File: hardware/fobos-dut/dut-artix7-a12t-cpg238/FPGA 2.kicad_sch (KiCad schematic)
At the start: 7 parts

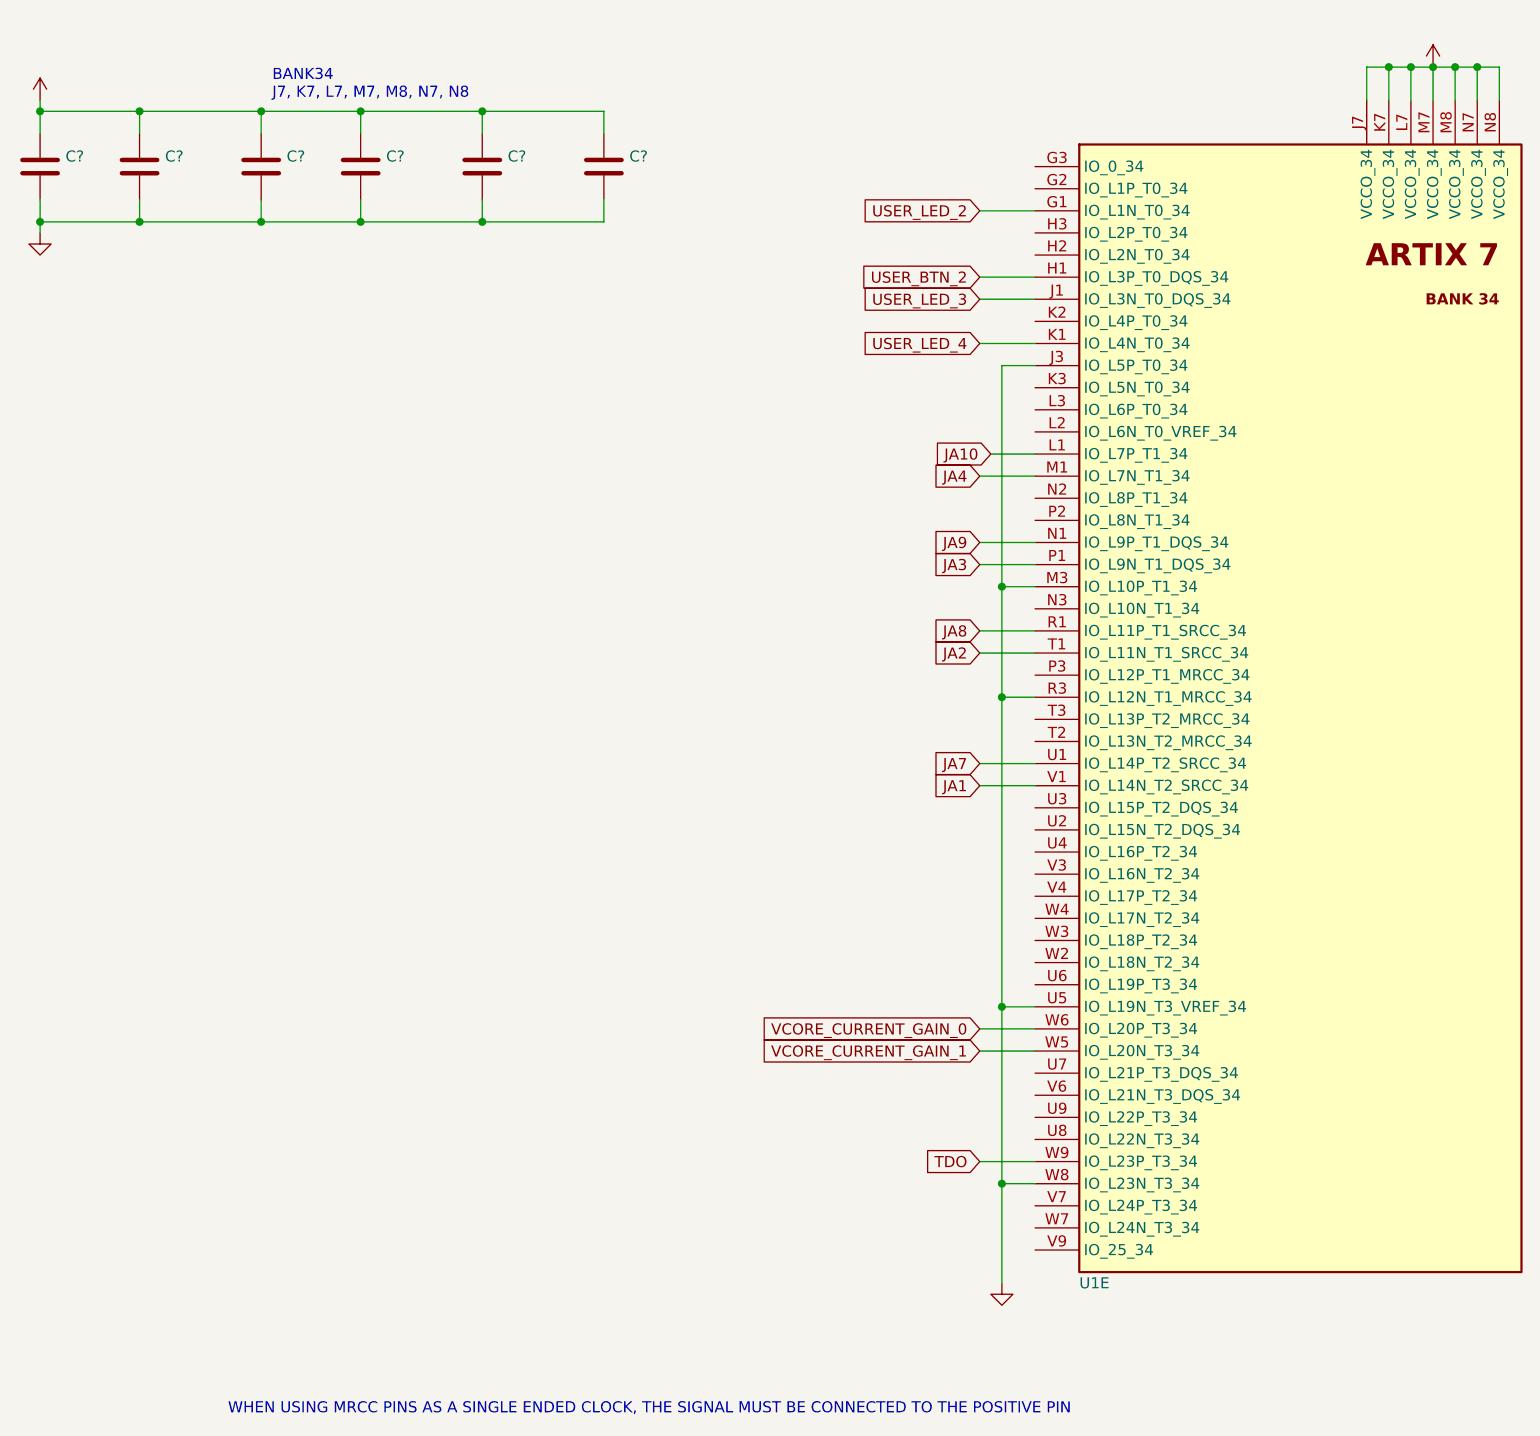
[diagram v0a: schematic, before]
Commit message: transitioned artix-7 dut to Kikad 6
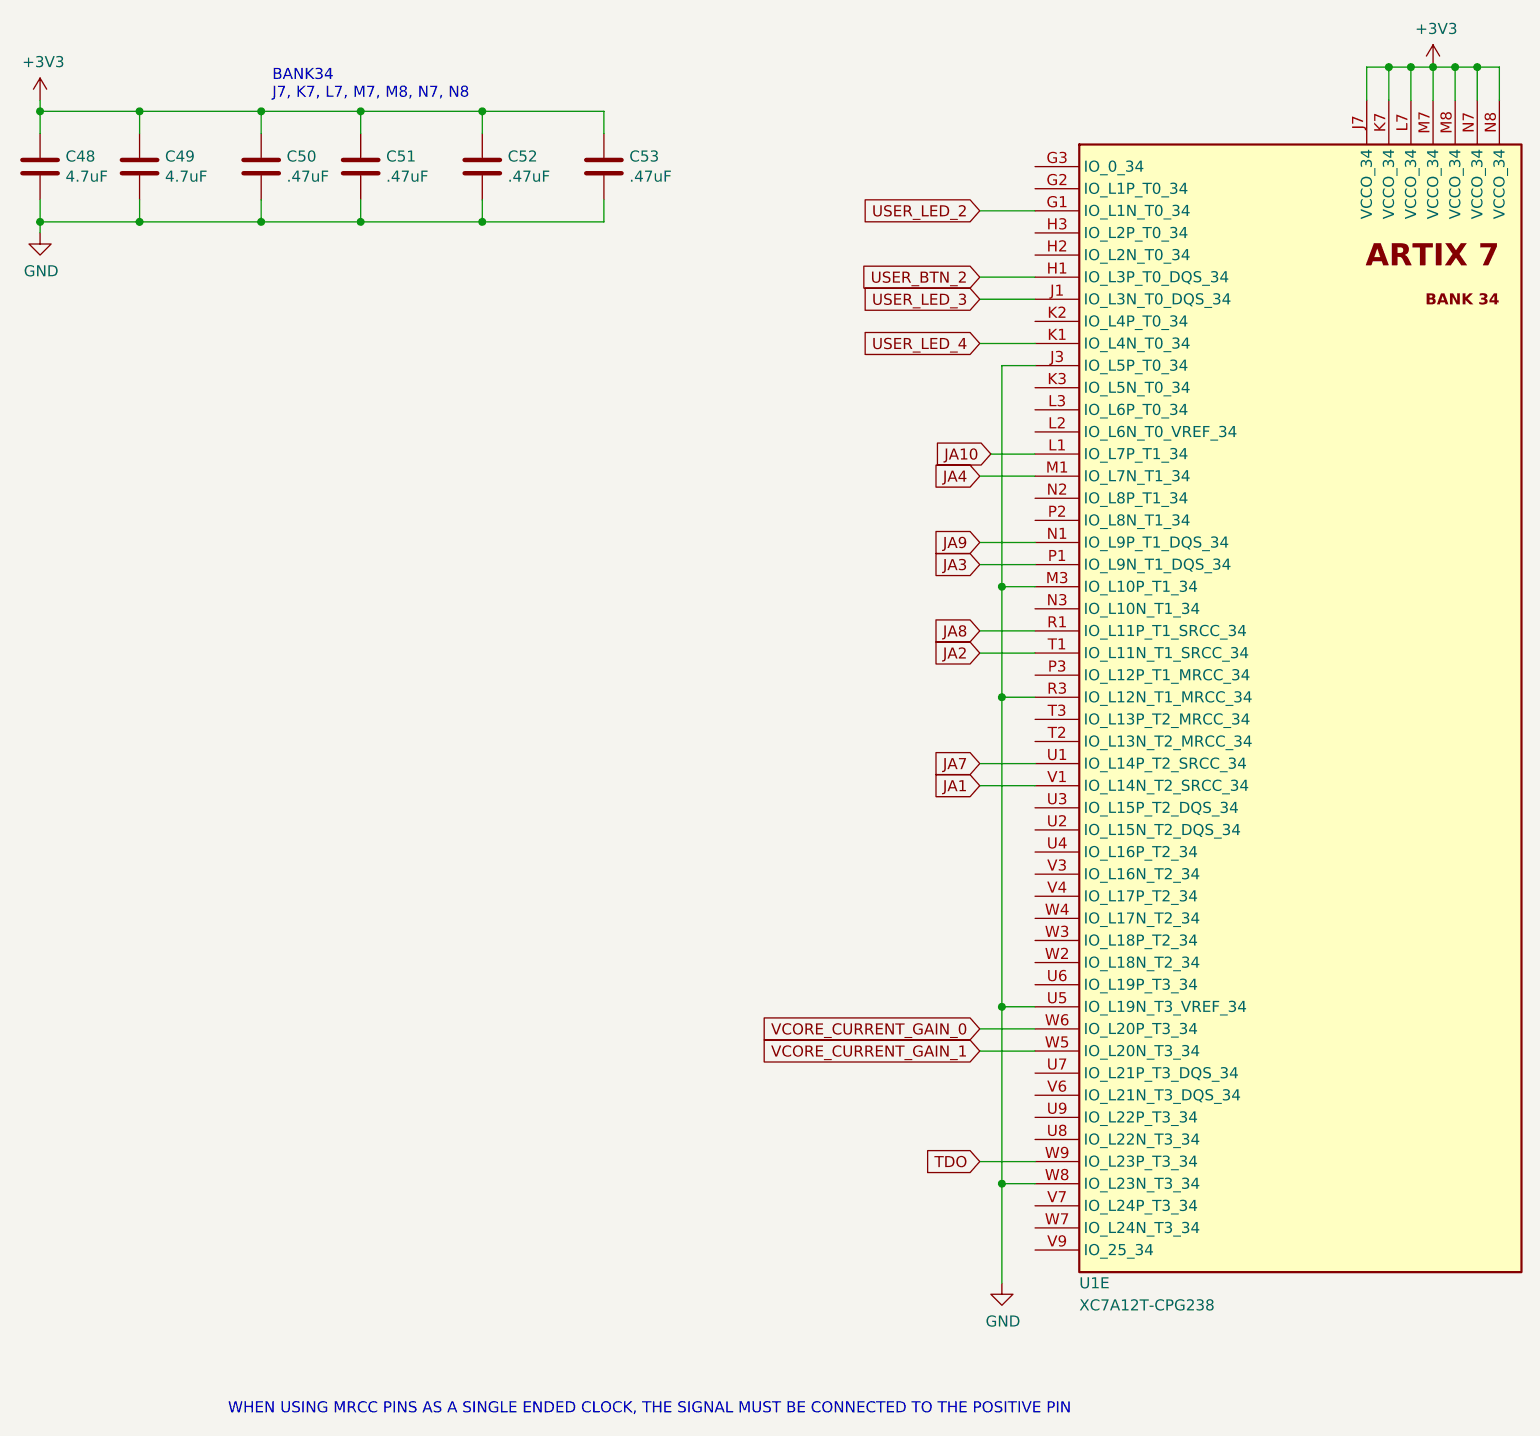
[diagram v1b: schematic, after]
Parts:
- C48, C49: renamed from C?; value (none) -> 4.7uF; footprint (none) -> Capacitor_SMD:C_0402_1005Metric_Pad0.74x0.62mm_HandSolder
- C50, C51, C52, C53: renamed from C?; value (none) -> .47uF; footprint (none) -> Capacitor_SMD:C_0402_1005Metric_Pad0.74x0.62mm_HandSolder
- U1: value (none) -> XC7A12T-CPG238; footprint (none) -> Package_BGA:Xilinx_CPG238
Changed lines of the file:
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@@
   (symbol (lib_id "power:+3V3") (at 179.07 20.32 0) (unit 1)
     (in_bom yes) (on_board yes)
-    (property "Reference" "#PWR?" (id 0) (at 179.07 24.13 0)
-      (effects (font (size 1.27 1.27)) hide)
-    )
-    (property "Value" "" (id 1) (at 179.451 15.9258 0))
+    (property "Reference" "#PWR0149" (id 0) (at 179.07 24.13 0)
+      (effects (font (size 1.27 1.27)) hide)
+    )
+    (property "Value" "+3V3" (id 1) (at 179.451 15.9258 0))
     (property "Footprint" "" (id 2) (at 179.07 20.32 0)
       (effects (font (size 1.27 1.27)) hide)
@@
       (effects (font (size 1.27 1.27)) (justify left))
     )
-    (property "Value" "" (id 1) (at 138.43 162.56 0)
-      (effects (font (size 1.27 1.27)) (justify left))
-    )
-    (property "Footprint" "" (id 2) (at 133.35 31.75 0)
+    (property "Value" "XC7A12T-CPG238" (id 1) (at 138.43 162.56 0)
+      (effects (font (size 1.27 1.27)) (justify left))
+    )
+    (property "Footprint" "Package_BGA:Xilinx_CPG238" (id 2) (at 133.35 31.75 0)
       (effects (font (size 1.27 1.27)) hide)
     )
@@
   (symbol (lib_id "Device:C") (at 19.05 31.75 0) (unit 1)
     (in_bom yes) (on_board yes)
-    (property "Reference" "C?" (id 0) (at 21.971 30.5816 0)
-      (effects (font (size 1.27 1.27)) (justify left))
-    )
-    (property "Value" "" (id 1) (at 21.971 32.893 0)
-      (effects (font (size 1.27 1.27)) (justify left))
-    )
-    (property "Footprint" "" (id 2) (at 20.0152 35.56 0)
+    (property "Reference" "C48" (id 0) (at 21.971 30.5816 0)
+      (effects (font (size 1.27 1.27)) (justify left))
+    )
+    (property "Value" "4.7uF" (id 1) (at 21.971 32.893 0)
+      (effects (font (size 1.27 1.27)) (justify left))
+    )
+    (property "Footprint" "Capacitor_SMD:C_0402_1005Metric_Pad0.74x0.62mm_HandSolder" (id 2) (at 20.0152 35.56 0)
       (effects (font (size 1.27 1.27)) hide)
     )
@@
   (symbol (lib_id "Device:C") (at 30.48 31.75 0) (unit 1)
     (in_bom yes) (on_board yes)
-    (property "Reference" "C?" (id 0) (at 33.401 30.5816 0)
-      (effects (font (size 1.27 1.27)) (justify left))
-    )
-    (property "Value" "" (id 1) (at 33.401 32.893 0)
-      (effects (font (size 1.27 1.27)) (justify left))
-    )
-    (property "Footprint" "" (id 2) (at 31.4452 35.56 0)
+    (property "Reference" "C49" (id 0) (at 33.401 30.5816 0)
+      (effects (font (size 1.27 1.27)) (justify left))
+    )
+    (property "Value" "4.7uF" (id 1) (at 33.401 32.893 0)
+      (effects (font (size 1.27 1.27)) (justify left))
+    )
+    (property "Footprint" "Capacitor_SMD:C_0402_1005Metric_Pad0.74x0.62mm_HandSolder" (id 2) (at 31.4452 35.56 0)
       (effects (font (size 1.27 1.27)) hide)
     )
@@
   (symbol (lib_id "Device:C") (at 44.45 31.75 0) (unit 1)
     (in_bom yes) (on_board yes)
-    (property "Reference" "C?" (id 0) (at 47.371 30.5816 0)
-      (effects (font (size 1.27 1.27)) (justify left))
-    )
-    (property "Value" "" (id 1) (at 47.371 32.893 0)
-      (effects (font (size 1.27 1.27)) (justify left))
-    )
-    (property "Footprint" "" (id 2) (at 45.4152 35.56 0)
+    (property "Reference" "C50" (id 0) (at 47.371 30.5816 0)
+      (effects (font (size 1.27 1.27)) (justify left))
+    )
+    (property "Value" ".47uF" (id 1) (at 47.371 32.893 0)
+      (effects (font (size 1.27 1.27)) (justify left))
+    )
+    (property "Footprint" "Capacitor_SMD:C_0402_1005Metric_Pad0.74x0.62mm_HandSolder" (id 2) (at 45.4152 35.56 0)
       (effects (font (size 1.27 1.27)) hide)
     )
@@
   (symbol (lib_id "Device:C") (at 55.88 31.75 0) (unit 1)
     (in_bom yes) (on_board yes)
-    (property "Reference" "C?" (id 0) (at 58.801 30.5816 0)
-      (effects (font (size 1.27 1.27)) (justify left))
-    )
-    (property "Value" "" (id 1) (at 58.801 32.893 0)
-      (effects (font (size 1.27 1.27)) (justify left))
-    )
-    (property "Footprint" "" (id 2) (at 56.8452 35.56 0)
+    (property "Reference" "C51" (id 0) (at 58.801 30.5816 0)
+      (effects (font (size 1.27 1.27)) (justify left))
+    )
+    (property "Value" ".47uF" (id 1) (at 58.801 32.893 0)
+      (effects (font (size 1.27 1.27)) (justify left))
+    )
+    (property "Footprint" "Capacitor_SMD:C_0402_1005Metric_Pad0.74x0.62mm_HandSolder" (id 2) (at 56.8452 35.56 0)
       (effects (font (size 1.27 1.27)) hide)
     )
@@
   (symbol (lib_id "Device:C") (at 69.85 31.75 0) (unit 1)
     (in_bom yes) (on_board yes)
-    (property "Reference" "C?" (id 0) (at 72.771 30.5816 0)
-      (effects (font (size 1.27 1.27)) (justify left))
-    )
-    (property "Value" "" (id 1) (at 72.771 32.893 0)
-      (effects (font (size 1.27 1.27)) (justify left))
-    )
-    (property "Footprint" "" (id 2) (at 70.8152 35.56 0)
+    (property "Reference" "C52" (id 0) (at 72.771 30.5816 0)
+      (effects (font (size 1.27 1.27)) (justify left))
+    )
+    (property "Value" ".47uF" (id 1) (at 72.771 32.893 0)
+      (effects (font (size 1.27 1.27)) (justify left))
+    )
+    (property "Footprint" "Capacitor_SMD:C_0402_1005Metric_Pad0.74x0.62mm_HandSolder" (id 2) (at 70.8152 35.56 0)
       (effects (font (size 1.27 1.27)) hide)
     )
@@
   (symbol (lib_id "Device:C") (at 83.82 31.75 0) (unit 1)
     (in_bom yes) (on_board yes)
-    (property "Reference" "C?" (id 0) (at 86.741 30.5816 0)
-      (effects (font (size 1.27 1.27)) (justify left))
-    )
-    (property "Value" "" (id 1) (at 86.741 32.893 0)
-      (effects (font (size 1.27 1.27)) (justify left))
-    )
-    (property "Footprint" "" (id 2) (at 84.7852 35.56 0)
+    (property "Reference" "C53" (id 0) (at 86.741 30.5816 0)
+      (effects (font (size 1.27 1.27)) (justify left))
+    )
+    (property "Value" ".47uF" (id 1) (at 86.741 32.893 0)
+      (effects (font (size 1.27 1.27)) (justify left))
+    )
+    (property "Footprint" "Capacitor_SMD:C_0402_1005Metric_Pad0.74x0.62mm_HandSolder" (id 2) (at 84.7852 35.56 0)
       (effects (font (size 1.27 1.27)) hide)
     )
@@
   (symbol (lib_id "power:GND") (at 19.05 39.37 0) (unit 1)
     (in_bom yes) (on_board yes)
-    (property "Reference" "#PWR?" (id 0) (at 19.05 45.72 0)
-      (effects (font (size 1.27 1.27)) hide)
-    )
-    (property "Value" "" (id 1) (at 19.177 43.7642 0))
+    (property "Reference" "#PWR055" (id 0) (at 19.05 45.72 0)
+      (effects (font (size 1.27 1.27)) hide)
+    )
+    (property "Value" "GND" (id 1) (at 19.177 43.7642 0))
     (property "Footprint" "" (id 2) (at 19.05 39.37 0)
       (effects (font (size 1.27 1.27)) hide)
@@
   (symbol (lib_id "power:+3V3") (at 19.05 24.13 0) (unit 1)
     (in_bom yes) (on_board yes)
-    (property "Reference" "#PWR?" (id 0) (at 19.05 27.94 0)
-      (effects (font (size 1.27 1.27)) hide)
-    )
-    (property "Value" "" (id 1) (at 19.431 19.7358 0))
+    (property "Reference" "#PWR054" (id 0) (at 19.05 27.94 0)
+      (effects (font (size 1.27 1.27)) hide)
+    )
+    (property "Value" "+3V3" (id 1) (at 19.431 19.7358 0))
     (property "Footprint" "" (id 2) (at 19.05 24.13 0)
       (effects (font (size 1.27 1.27)) hide)
@@
   (symbol (lib_id "power:GND") (at 129.54 160.02 0) (unit 1)
     (in_bom yes) (on_board yes)
-    (property "Reference" "#PWR?" (id 0) (at 129.54 166.37 0)
-      (effects (font (size 1.27 1.27)) hide)
-    )
-    (property "Value" "" (id 1) (at 129.667 164.4142 0))
+    (property "Reference" "#PWR0135" (id 0) (at 129.54 166.37 0)
+      (effects (font (size 1.27 1.27)) hide)
+    )
+    (property "Value" "GND" (id 1) (at 129.667 164.4142 0))
     (property "Footprint" "" (id 2) (at 129.54 160.02 0)
       (effects (font (size 1.27 1.27)) hide)
